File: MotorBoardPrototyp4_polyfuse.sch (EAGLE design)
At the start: 88 parts, among them IC1 OPA4340E, IC2 OPA4340E

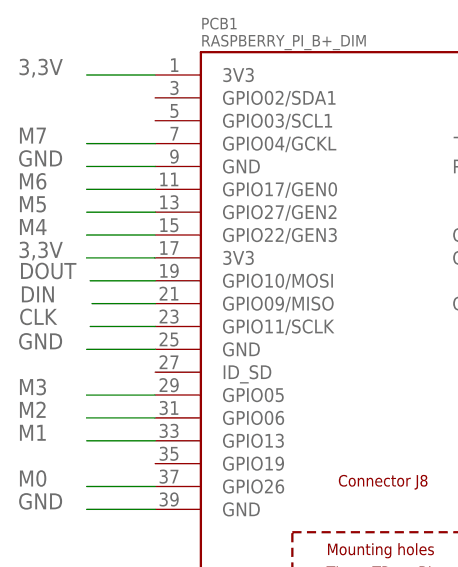
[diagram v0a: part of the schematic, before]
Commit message: corrected MISO and MOSI closes #2
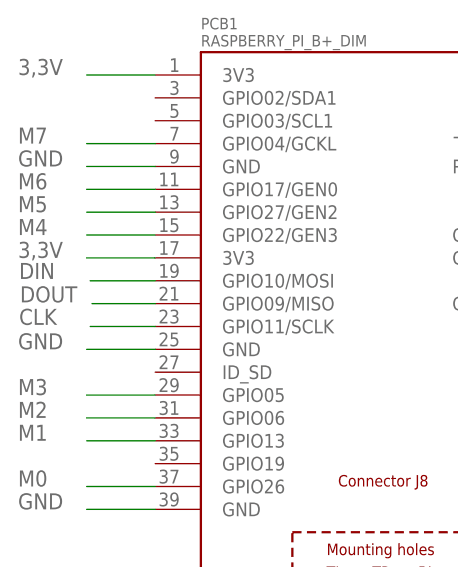
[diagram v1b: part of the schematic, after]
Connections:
- net DIN: now also PCB1.GPIO10/MOSI; no longer PCB1.GPIO09/MISO
- net DOUT: now also PCB1.GPIO09/MISO; no longer PCB1.GPIO10/MOSI
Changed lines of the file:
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@@
 <grid distance="0.1" unitdist="inch" unit="inch" style="lines" multiple="1" display="no" altdistance="0.01" altunitdist="inch" altunit="inch"/>
 <layers>
-<layer number="1" name="Top" color="4" fill="1" visible="yes" active="no"/>
-<layer number="16" name="Bottom" color="1" fill="1" visible="yes" active="no"/>
-<layer number="17" name="Pads" color="2" fill="1" visible="yes" active="no"/>
-<layer number="18" name="Vias" color="2" fill="1" visible="yes" active="no"/>
-<layer number="19" name="Unrouted" color="6" fill="1" visible="yes" active="no"/>
-<layer number="20" name="Dimension" color="15" fill="1" visible="yes" active="no"/>
-<layer number="21" name="tPlace" color="7" fill="1" visible="yes" active="no"/>
-<layer number="22" name="bPlace" color="7" fill="1" visible="yes" active="no"/>
-<layer number="23" name="tOrigins" color="15" fill="1" visible="yes" active="no"/>
-<layer number="24" name="bOrigins" color="15" fill="1" visible="yes" active="no"/>
-<layer number="25" name="tNames" color="7" fill="1" visible="yes" active="no"/>
-<layer number="26" name="bNames" color="7" fill="1" visible="yes" active="no"/>
-<layer number="27" name="tValues" color="7" fill="1" visible="yes" active="no"/>
-<layer number="28" name="bValues" color="7" fill="1" visible="yes" active="no"/>
+<layer number="1" name="Top" color="4" fill="1" visible="no" active="no"/>
+<layer number="16" name="Bottom" color="1" fill="1" visible="no" active="no"/>
+<layer number="17" name="Pads" color="2" fill="1" visible="no" active="no"/>
+<layer number="18" name="Vias" color="2" fill="1" visible="no" active="no"/>
+<layer number="19" name="Unrouted" color="6" fill="1" visible="no" active="no"/>
+<layer number="20" name="Dimension" color="15" fill="1" visible="no" active="no"/>
+<layer number="21" name="tPlace" color="7" fill="1" visible="no" active="no"/>
+<layer number="22" name="bPlace" color="7" fill="1" visible="no" active="no"/>
+<layer number="23" name="tOrigins" color="15" fill="1" visible="no" active="no"/>
+<layer number="24" name="bOrigins" color="15" fill="1" visible="no" active="no"/>
+<layer number="25" name="tNames" color="7" fill="1" visible="no" active="no"/>
+<layer number="26" name="bNames" color="7" fill="1" visible="no" active="no"/>
+<layer number="27" name="tValues" color="7" fill="1" visible="no" active="no"/>
+<layer number="28" name="bValues" color="7" fill="1" visible="no" active="no"/>
 <layer number="29" name="tStop" color="7" fill="3" visible="no" active="no"/>
 <layer number="30" name="bStop" color="7" fill="6" visible="no" active="no"/>
@@
 <layer number="35" name="tGlue" color="7" fill="4" visible="no" active="no"/>
 <layer number="36" name="bGlue" color="7" fill="5" visible="no" active="no"/>
-<layer number="37" name="tTest" color="7" fill="1" visible="yes" active="no"/>
-<layer number="38" name="bTest" color="7" fill="1" visible="yes" active="no"/>
+<layer number="37" name="tTest" color="7" fill="1" visible="no" active="no"/>
+<layer number="38" name="bTest" color="7" fill="1" visible="no" active="no"/>
 <layer number="39" name="tKeepout" color="4" fill="11" visible="no" active="no"/>
 <layer number="40" name="bKeepout" color="1" fill="11" visible="no" active="no"/>
@@
 <layer number="44" name="Drills" color="7" fill="1" visible="no" active="no"/>
 <layer number="45" name="Holes" color="7" fill="1" visible="no" active="no"/>
-<layer number="46" name="Milling" color="3" fill="1" visible="yes" active="no"/>
-<layer number="47" name="Measures" color="7" fill="1" visible="yes" active="no"/>
-<layer number="48" name="Document" color="7" fill="1" visible="yes" active="no"/>
-<layer number="49" name="Reference" color="7" fill="1" visible="yes" active="no"/>
-<layer number="51" name="tDocu" color="7" fill="1" visible="yes" active="no"/>
-<layer number="52" name="bDocu" color="7" fill="1" visible="yes" active="no"/>
+<layer number="46" name="Milling" color="3" fill="1" visible="no" active="no"/>
+<layer number="47" name="Measures" color="7" fill="1" visible="no" active="no"/>
+<layer number="48" name="Document" color="7" fill="1" visible="no" active="no"/>
+<layer number="49" name="Reference" color="7" fill="1" visible="no" active="no"/>
+<layer number="51" name="tDocu" color="7" fill="1" visible="no" active="no"/>
+<layer number="52" name="bDocu" color="7" fill="1" visible="no" active="no"/>
 <layer number="90" name="Modules" color="5" fill="1" visible="yes" active="yes"/>
 <layer number="91" name="Nets" color="2" fill="1" visible="yes" active="yes"/>
@@
 </segment>
 <segment>
+<pinref part="PCB1" gate="G$1" pin="GPIO10/MOSI"/>
+<wire x1="-5.08" y1="63.5" x2="-12.3" y2="63.5" width="0.1524" layer="91"/>
+<label x="-20.2" y="63.7" size="1.778" layer="95"/>
+</segment>
+</net>
+<net name="DOUT" class="0">
+<segment>
+<pinref part="U$58" gate="G$1" pin="DOUT"/>
+<wire x1="383.54" y1="-14.7" x2="387" y2="-14.7" width="0.1524" layer="91"/>
+<label x="389.6" y="-14.7" size="1.778" layer="95"/>
+</segment>
+<segment>
 <pinref part="PCB1" gate="G$1" pin="GPIO09/MISO"/>
 <wire x1="-5.08" y1="60.96" x2="-12.1" y2="60.96" width="0.1524" layer="91"/>
@@
 </segment>
 </net>
-<net name="DOUT" class="0">
-<segment>
-<pinref part="U$58" gate="G$1" pin="DOUT"/>
-<wire x1="383.54" y1="-14.7" x2="387" y2="-14.7" width="0.1524" layer="91"/>
-<label x="389.6" y="-14.7" size="1.778" layer="95"/>
-</segment>
-<segment>
-<pinref part="PCB1" gate="G$1" pin="GPIO10/MOSI"/>
-<wire x1="-5.08" y1="63.5" x2="-12.3" y2="63.5" width="0.1524" layer="91"/>
-<label x="-20.2" y="63.7" size="1.778" layer="95"/>
-</segment>
-</net>
